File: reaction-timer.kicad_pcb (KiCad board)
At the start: 2 copper layers, 48 x 80 mm, 38 parts, among them IC1 4026, IC2 4026, IC3 4026, IC5 NE555P, IC6 NE555P, IC7 NE555P

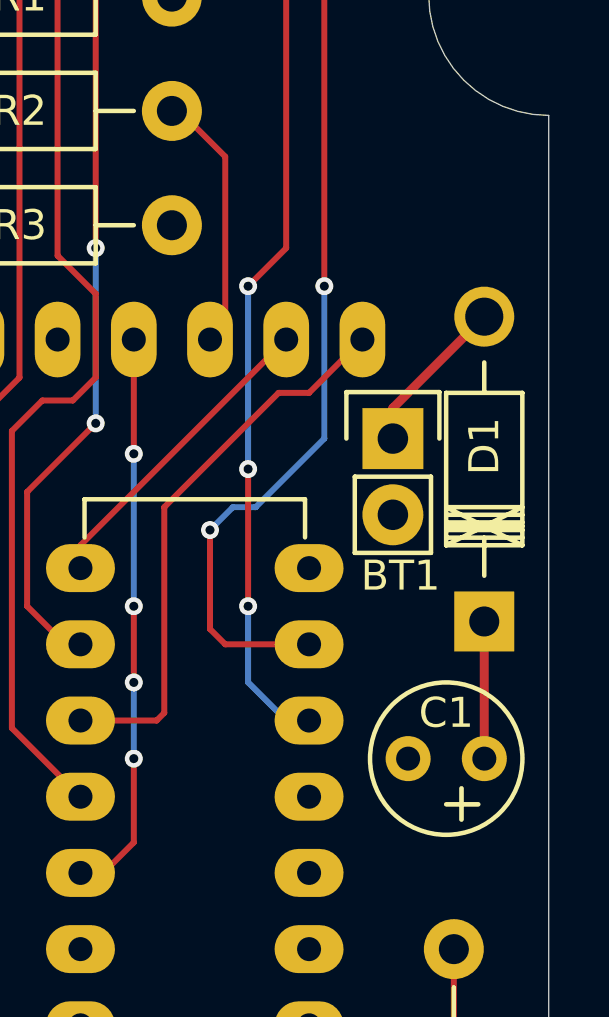
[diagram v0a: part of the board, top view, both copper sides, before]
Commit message: Move power input
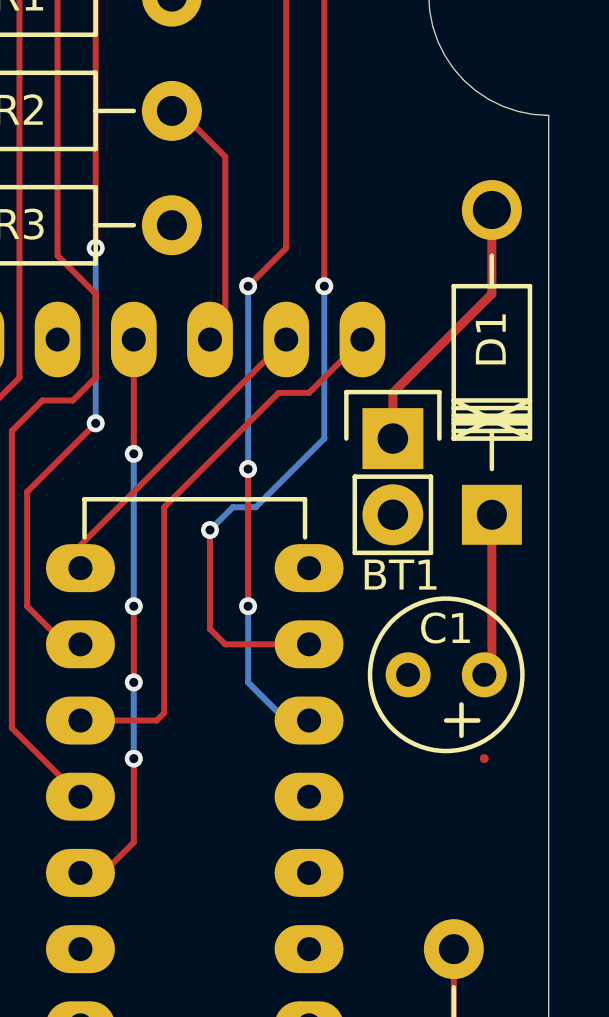
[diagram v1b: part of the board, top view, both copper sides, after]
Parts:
- moved D1 3.57 mm to (103.4, 84.6)
- moved C1 2.79 mm to (103.1, 89.9)
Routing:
- net +9V: track 5.33 -> 8.99 mm
- net Net-(C1-Pad1): track 18.9 -> 19.8 mm
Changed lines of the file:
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@@
     (thickness 1.6)
     (drawings 8)
-    (tracks 266)
+    (tracks 268)
     (zones 0)
     (modules 38)
@@
   )
   (module Capacitors_Elko_ThroughHole:Elko_vert_11x5mm_RM2.5 (layer F.Cu)
-    (at 103.124 92.71 180)
+    (at 103.124 89.916 180)
     (descr "Electrolytic Capacitor, vertical, diameter 5mm, radial, RM 2,5mm")
     (tags "Electrolytic Capacitor, vertical, diameter 5mm, radial, RM 2,5mm, Elko, Electrolytkondensator, Kondensator gepolt, Durchmesser 5mm")
@@
   )
   (module Diodes_ThroughHole:Diode_DO-41_SOD81_Horizontal_RM10 (layer F.Cu)
-    (at 103.124 88.138 90)
+    (at 103.378 84.582 90)
     (descr "Diode, DO-41, SOD81, Horizontal, RM 10mm,")
     (tags "Diode, DO-41, SOD81, Horizontal, RM 10mm, 1N4007, SB140,")
@@
   (gr_line (start 101.27 61.27) (end 101.27 67.27) (angle 90) (layer Edge.Cuts) (width 0.001))
   (gr_line (start 61.27 61.27) (end 101.27 61.27) (angle 90) (layer Edge.Cuts) (width 0.001))
+  (segment (start 103.12146 92.70746) (end 103.124 92.71) (width 0.3) (layer F.Cu) (net 0))
   (segment (start 89.662 91.44) (end 92.202 91.44) (width 0.2) (layer F.Cu) (net 1))
   (segment (start 97.282 80.518) (end 99.06 78.74) (width 0.2) (layer F.Cu) (net 1))
@@
   (segment (start 73.66 88.9) (end 74.676 87.884) (width 0.2) (layer F.Cu) (net 30))
   (segment (start 72.39 88.9) (end 73.66 88.9) (width 0.2) (layer F.Cu) (net 30))
-  (segment (start 100.076 82.042) (end 100.076 81.02346) (width 0.3) (layer F.Cu) (net 31))
-  (segment (start 100.076 81.02346) (end 103.12146 77.978) (width 0.3) (layer F.Cu) (net 31))
-  (segment (start 103.12146 88.138) (end 103.12146 92.70746) (width 0.3) (layer F.Cu) (net 33) (status C00000))
-  (segment (start 103.12146 92.70746) (end 103.124 92.71) (width 0.3) (layer F.Cu) (net 33) (status C00000))
+  (segment (start 100.076 82.042) (end 100.076 80.518) (width 0.3) (layer F.Cu) (net 31) (status 400000))
+  (segment (start 103.37546 77.21854) (end 103.37546 74.422) (width 0.3) (layer F.Cu) (net 31) (status 800000))
+  (segment (start 100.076 80.518) (end 103.37546 77.21854) (width 0.3) (layer F.Cu) (net 31))
+  (segment (start 103.37546 84.582) (end 103.37546 89.66454) (width 0.3) (layer F.Cu) (net 33) (status C00000))
+  (segment (start 103.37546 89.66454) (end 103.124 89.916) (width 0.3) (layer F.Cu) (net 33) (status C00000))
   (segment (start 97.282 111.252) (end 97.536 111.252) (width 0.2) (layer F.Cu) (net 33))
   (segment (start 97.536 111.252) (end 102.108 106.68) (width 0.2) (layer F.Cu) (net 33))

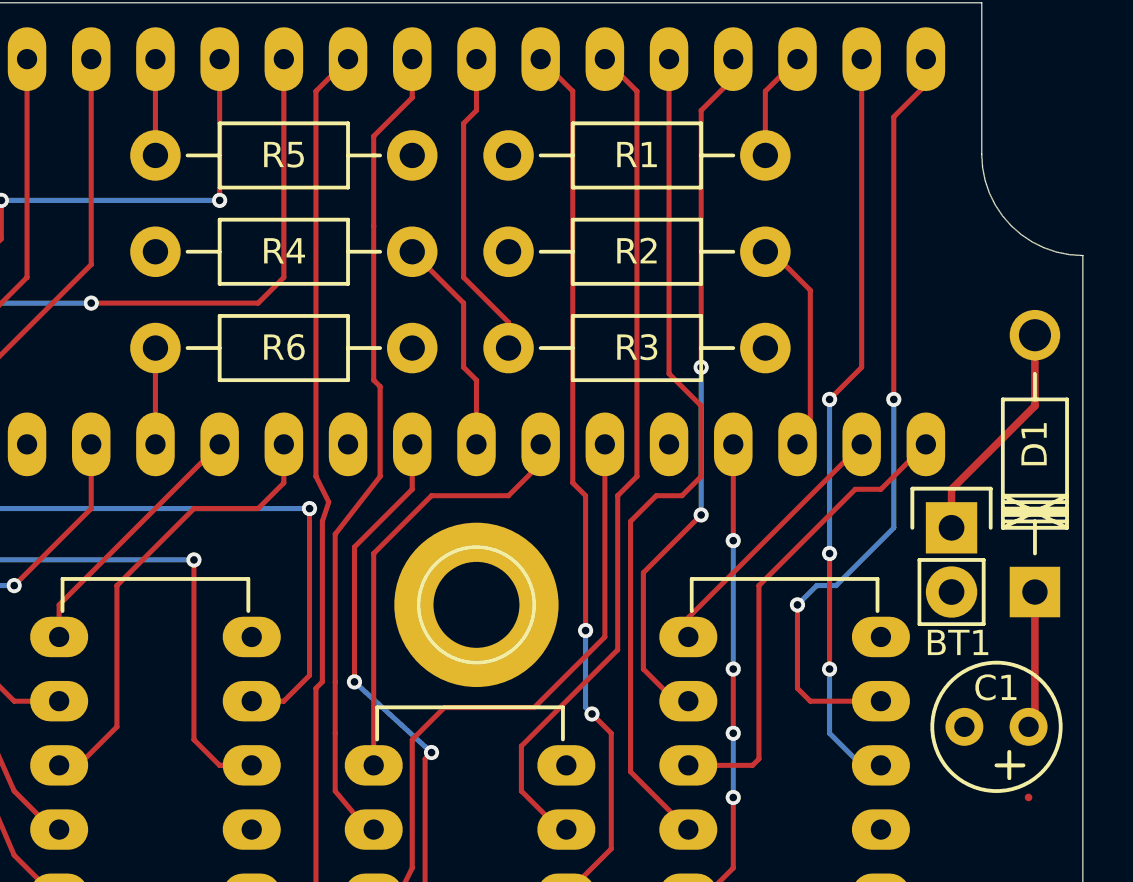
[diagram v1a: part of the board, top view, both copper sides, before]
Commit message: Connect Vcc to the 7-seg display, but notice a problem!
- I've connected the displays as common anode, not common cathode (as
  they should be).
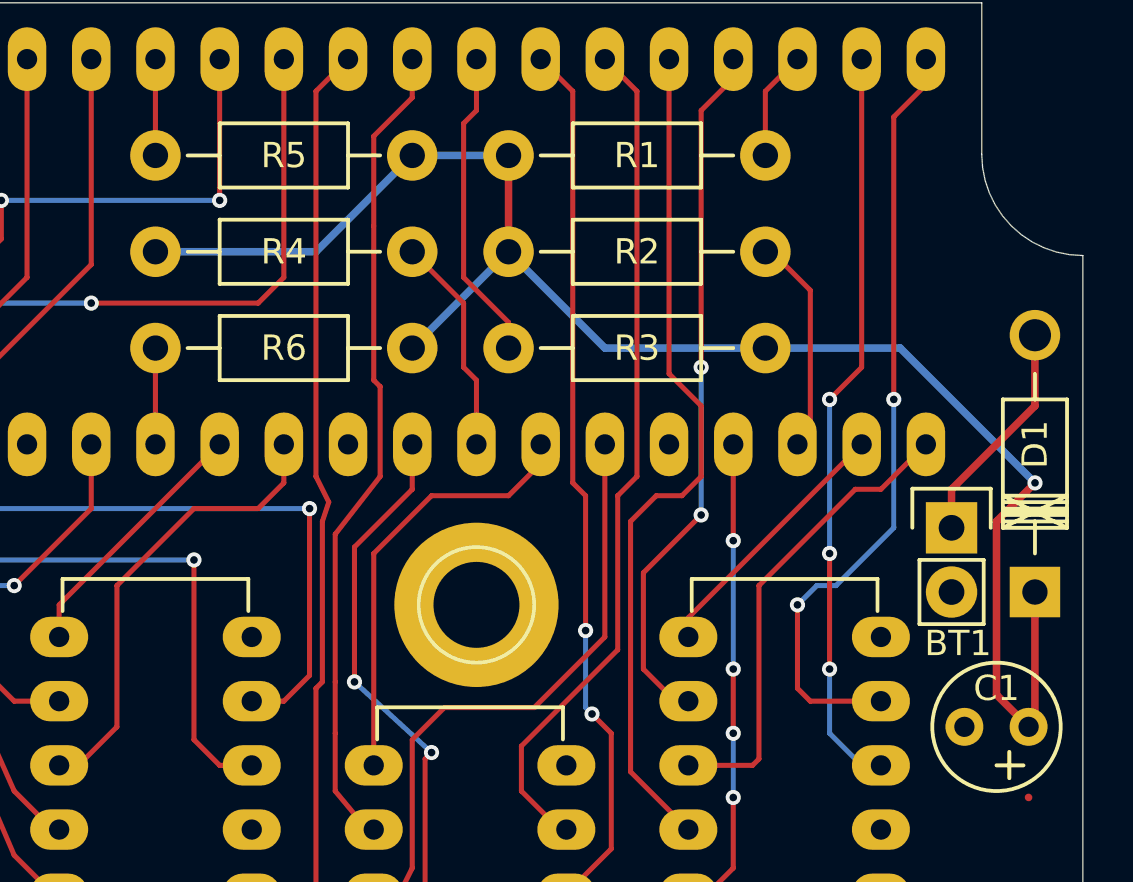
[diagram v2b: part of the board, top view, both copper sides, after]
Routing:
- net Net-(C1-Pad1): track 19.8 -> 79.9 mm, vias 0 -> 1
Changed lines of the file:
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@@
   (general
     (links 104)
-    (no_connects 49)
+    (no_connects 43)
     (area 57.269499 61.269499 105.270501 141.270501)
     (thickness 1.6)
     (drawings 8)
-    (tracks 268)
+    (tracks 281)
     (zones 0)
     (modules 38)
@@
   (segment (start 103.37546 77.21854) (end 103.37546 74.422) (width 0.3) (layer F.Cu) (net 31) (status 800000))
   (segment (start 100.076 80.518) (end 103.37546 77.21854) (width 0.3) (layer F.Cu) (net 31))
+  (segment (start 82.55 67.31) (end 82.55 71.12) (width 0.3) (layer F.Cu) (net 33) (status C00000))
+  (segment (start 68.58 71.12) (end 74.93 71.12) (width 0.3) (layer B.Cu) (net 33) (status 400000))
+  (segment (start 74.93 71.12) (end 78.74 67.31) (width 0.3) (layer B.Cu) (net 33) (status 800000))
+  (segment (start 82.55 71.12) (end 78.74 74.93) (width 0.3) (layer B.Cu) (net 33) (status C00000))
+  (segment (start 82.55 67.31) (end 78.74 67.31) (width 0.3) (layer B.Cu) (net 33) (status C00000))
+  (segment (start 92.71 74.93) (end 86.36 74.93) (width 0.3) (layer B.Cu) (net 33) (status 400000))
+  (segment (start 86.36 74.93) (end 82.55 71.12) (width 0.3) (layer B.Cu) (net 33) (status 800000))
+  (segment (start 103.124 89.916) (end 101.854 88.646) (width 0.3) (layer F.Cu) (net 33) (status 400000))
+  (segment (start 98.044 74.93) (end 92.71 74.93) (width 0.3) (layer B.Cu) (net 33) (status 800000))
+  (segment (start 103.378 80.264) (end 98.044 74.93) (width 0.3) (layer B.Cu) (net 33))
+  (via (at 103.378 80.264) (size 0.6) (layers F.Cu B.Cu) (net 33))
+  (segment (start 101.854 81.788) (end 103.378 80.264) (width 0.3) (layer F.Cu) (net 33))
+  (segment (start 101.854 88.646) (end 101.854 81.788) (width 0.3) (layer F.Cu) (net 33))
   (segment (start 103.37546 84.582) (end 103.37546 89.66454) (width 0.3) (layer F.Cu) (net 33) (status C00000))
   (segment (start 103.37546 89.66454) (end 103.124 89.916) (width 0.3) (layer F.Cu) (net 33) (status C00000))

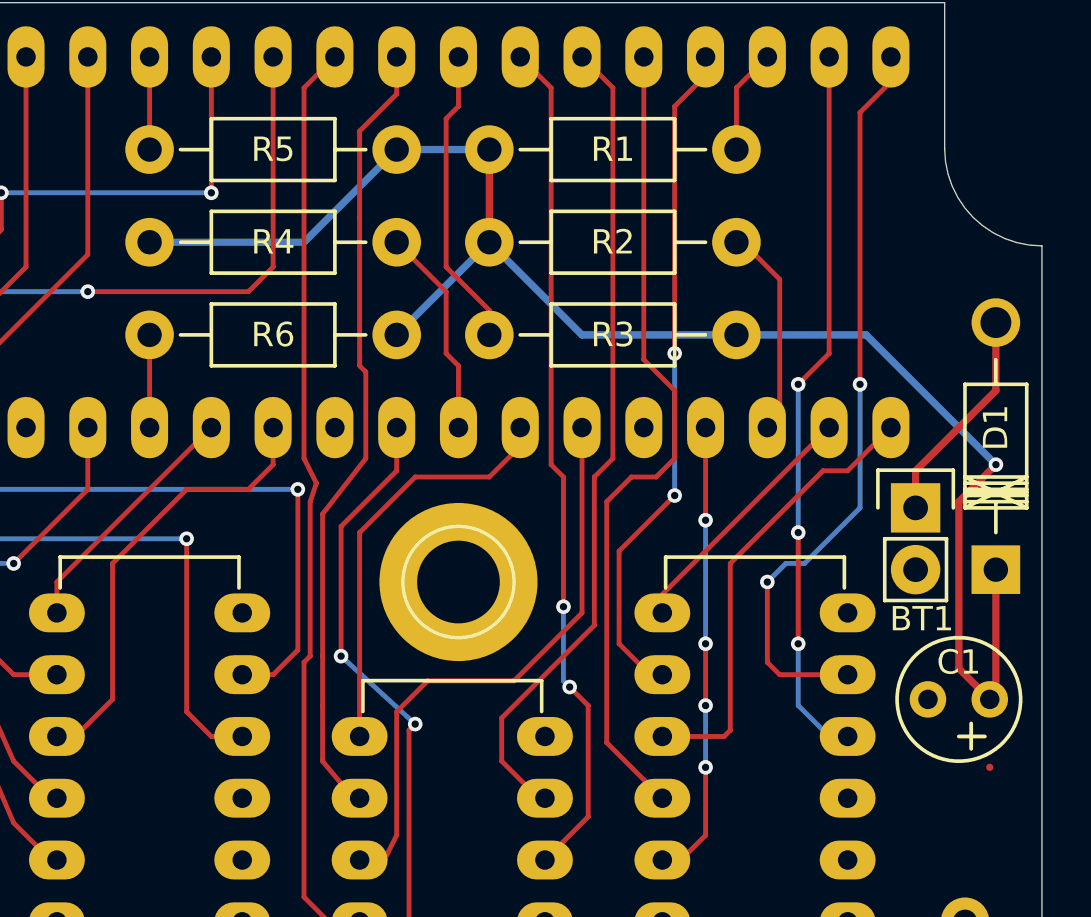
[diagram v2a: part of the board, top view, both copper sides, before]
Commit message: Fix PCB according to new netlist
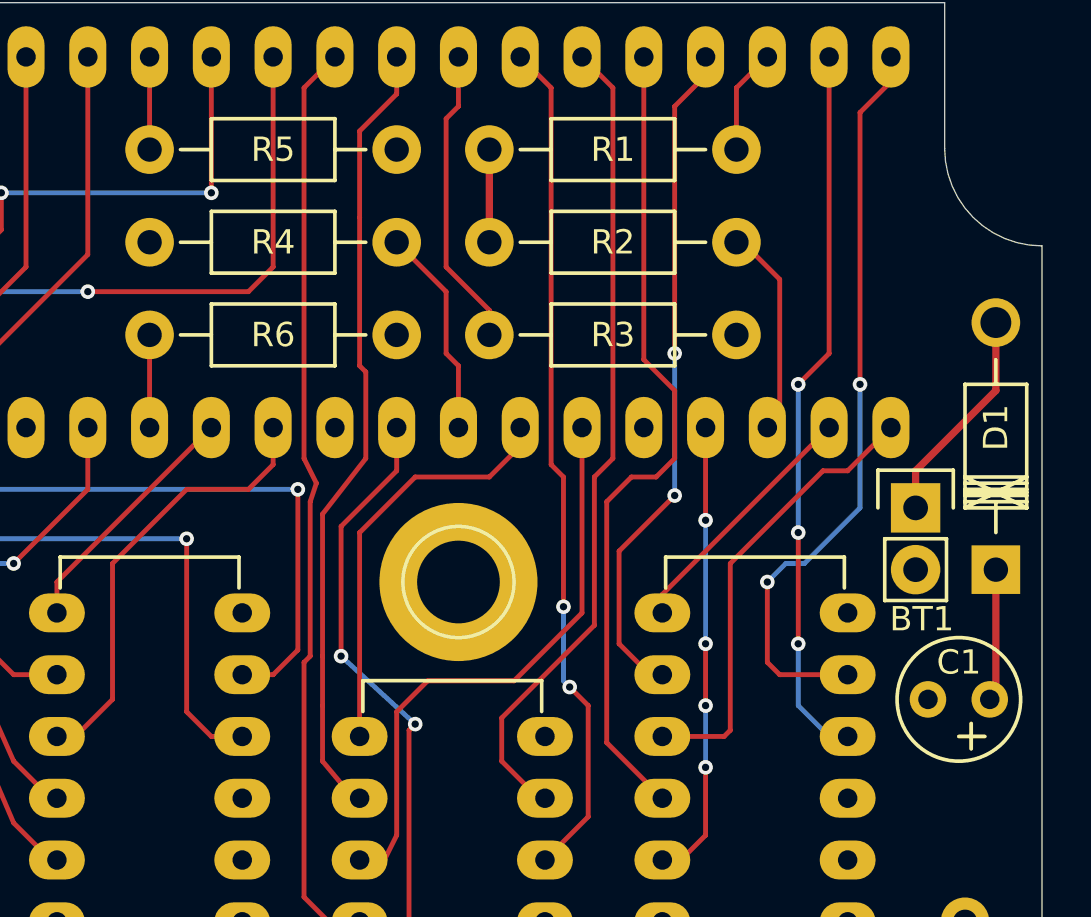
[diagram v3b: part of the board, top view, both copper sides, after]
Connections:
- R1 pad 1: Net-(C1-Pad1) -> GND
- R2 pad 1: Net-(C1-Pad1) -> GND
- R3 pad 1: Net-(C1-Pad1) -> GND
- R4 pad 1: Net-(C1-Pad1) -> GND
- R5 pad 1: Net-(C1-Pad1) -> GND
- R6 pad 1: Net-(C1-Pad1) -> GND
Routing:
- net Net-(C1-Pad1): track 79.9 -> 19.8 mm, vias 1 -> 0
- net GND: track 0.00 -> 3.81 mm
